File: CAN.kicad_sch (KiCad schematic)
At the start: 32 parts, among them U7 MCP2515-xST, U8 SN65HVD230, Y1 16MHz

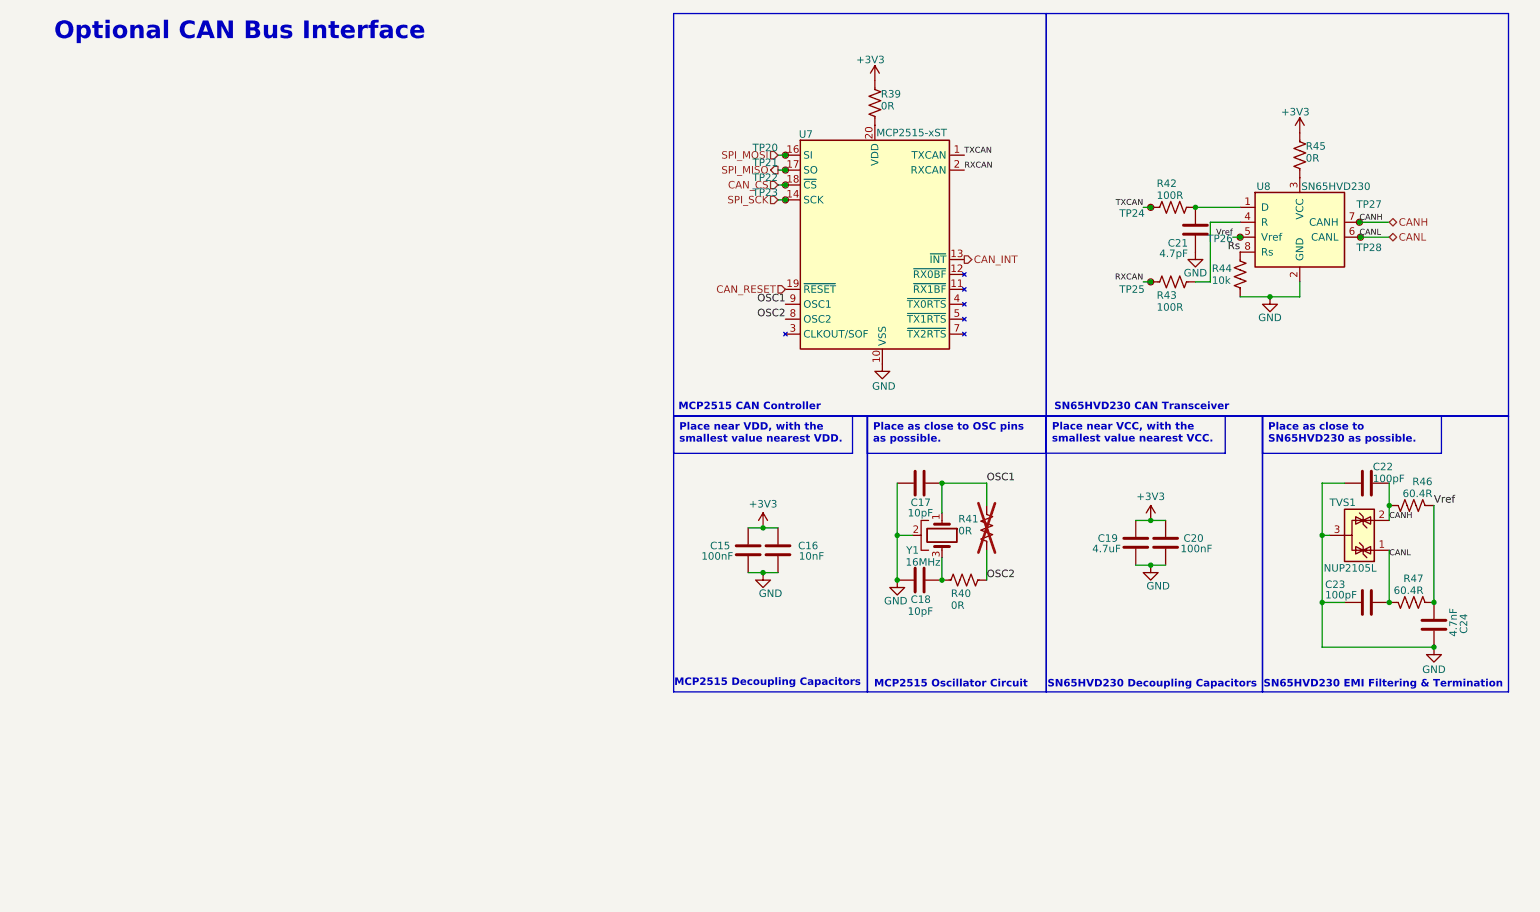
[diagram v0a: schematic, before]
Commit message: Added Graph & cleaned up title and layout
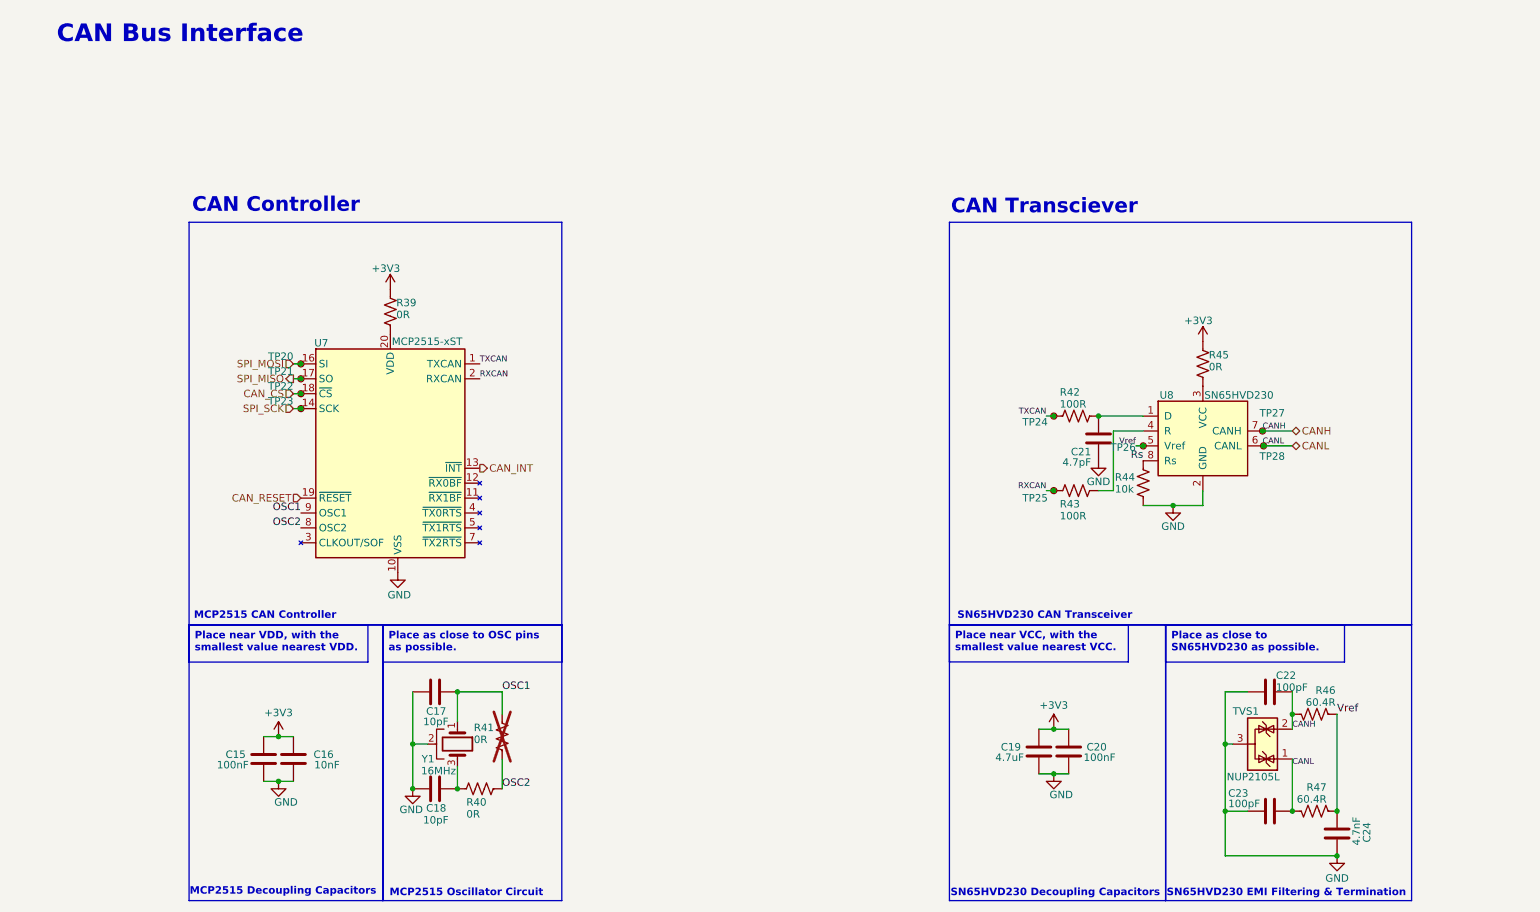
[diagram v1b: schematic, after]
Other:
- note added: "CAN Bus Interface"
- note added: "CAN Controller"
- note added: "CAN Transciever"
- note removed: "Optional CAN Bus Interface"
- company: FETfox -> github.com/FETfox/Li-Ion_Power_Module
- title: Li Lion Power Module -> Li Lion Power Module w/ Optional Fuel Gauge &CAN Bus
- moved on the sheet: C15, C16, C17, C18, C19, C20, C21, C22, C23, C24, R39, R40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
